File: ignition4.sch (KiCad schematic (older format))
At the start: 9 parts, among them P10 CONN_1, P11 CONN_1, Q3 MOSFET_N, SW3 SWITCH_INV

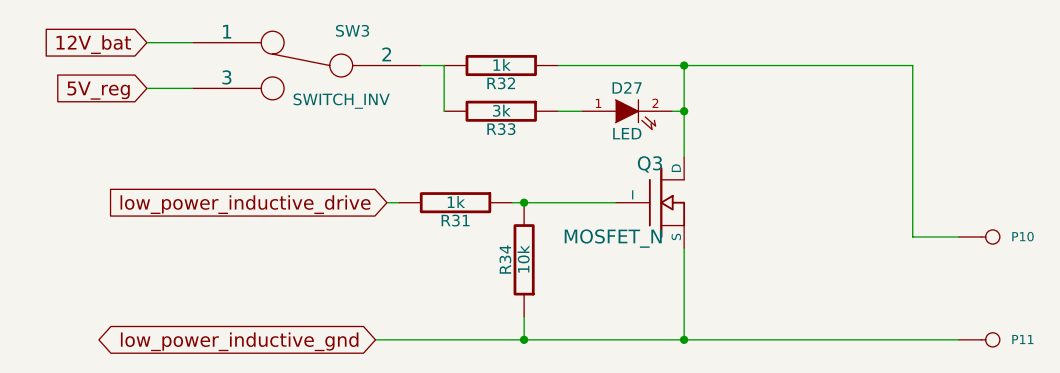
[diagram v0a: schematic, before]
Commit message: DFH mans up a bit. Perhaps usable for something at this point, like making trips to the local store ;)
I connected TA pins to sub circuits, fixed a number if items discussed in the DIYEFI forums. This is it's 21st version, so it was time for it to man up a bit, and become something potentially useful.

Signed-off-by: Jared Harvey <TortiseGIT@jaredharvey.com>
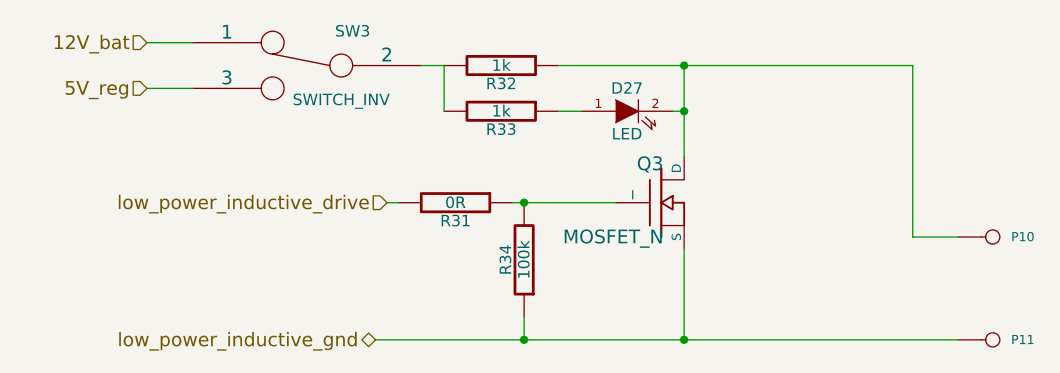
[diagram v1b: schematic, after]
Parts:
- D27: A (none) -> 10mA; V (none) -> 12V; construct (none) -> LED with resistor included; misc (none) -> other,more,stuff; vend1,smd e hem (none) -> newark,; vend2, smd w hem (none) -> digi,; vend2, thru w hem (none) -> digi,; vendor1, thru e hem (none) -> newark,58K2517
- Q3: A (none) -> 28A; V (none) -> 42V; construct (none) -> OVP protected MOSFET; misc (none) -> other,more,stuff; vend1,smd e hem (none) -> newark,; vend2, smd w hem (none) -> digi,; vend2, thru w hem (none) -> digi,VNP28N04-E-ND; vendor1, thru e hem (none) -> element14,1739427
- R31: value 1k -> 0R; TOL (none) -> 5%; W (none) -> 1/4W; construct (none) -> carbon film; misc (none) -> other,more,stuff; vend1,smd e hem (none) -> newark,36C9353; vend2, smd w hem (none) -> digi,CRCW08050000ZSTA-ND; vend2, thru w hem (none) -> digi,604HR025E-ND; vendor1, thru e hem (none) -> newark,64K9335
- R32: W (none) -> 1/4w; construct (none) -> carbon film; misc (none) -> other,more,stuff; tol (none) -> 5%; vend1,smd e hem (none) -> newark,52K9725; vend2, smd w hem (none) -> digi,CRCW08051K00JNEA; vend2, thru w hem (none) -> digi,OD102J-ND; vendor1, thru e hem (none) -> newark,65K2365
- R33: value 3k -> 1k; W (none) -> 1/4w; construct (none) -> carbon film; misc (none) -> other,more,stuff; tol (none) -> 5%; vend1,smd e hem (none) -> newark,52K9725; vend2, smd w hem (none) -> digi,CRCW08051K00JNEA; vend2, thru w hem (none) -> digi,OD102J-ND; vendor1, thru e hem (none) -> newark,65K2365
- R34: value 10k -> 100k; Field10 (none) -> carbon film; Field11 (none) -> other,more,stuff; Field4 (none) -> newark,38k0328; Field5 (none) -> vendor1, smd w hem; Field6 (none) -> vendor2, thru w hem; Field7 (none) -> vendor2, smd w hem; Field8 (none) -> 250,mW; Field9 (none) -> 5,%
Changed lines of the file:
@@
-EESchema Schematic File Version 1
-LIBS:power,./freeEMS_lib,device,conn,linear,regul,74xx,cmos4000,adc-dac,memory,xilinx,special,microcontrollers,dsp,microchip,analog_switches,motorola,texas,intel,audio,interface,digital-audio,philips,display,cypress,siliconi,contrib,valves,./freeEMS_1.cache
-EELAYER 23  0
+EESchema Schematic File Version 2  date 9/10/2011 11:43:50 AM
+LIBS:power
+LIBS:freeEMS_lib
+LIBS:device
+LIBS:conn
+LIBS:linear
+LIBS:regul
+LIBS:74xx
+LIBS:cmos4000
+LIBS:adc-dac
+LIBS:memory
+LIBS:xilinx
+LIBS:special
+LIBS:microcontrollers
+LIBS:dsp
+LIBS:microchip
+LIBS:analog_switches
+LIBS:motorola
+LIBS:texas
+LIBS:intel
+LIBS:audio
+LIBS:interface
+LIBS:digital-audio
+LIBS:philips
+LIBS:display
+LIBS:cypress
+LIBS:siliconi
+LIBS:contrib
+LIBS:valves
+LIBS:freeEMS_1-cache
+EELAYER 25  0
 EELAYER END
 $Descr A4 11700 8267
+encoding utf-8
 Sheet 12 41
-Title "freeEMS 1.0"
-Date "15 nov 2008"
-Rev "A.20"
-Comp "diyefi.org"
+Title "DFH for freeEMS"
+Date "10 sep 2011"
+Rev "A.21"
+Comp "FreeEMS.org"
 Comment1 "ignition.sch"
 Comment2 ""
@@
 $Comp
 L PIP-3104 Q3
-U 1 1 48B16ED5
+U 1 1 4E6B707C
 P 4000 2050
-F 0 "Q3" H 4010 2220 60  0000 R C
-F 1 "MOSFET_N" H 4010 1900 60  0000 R C
-F 2 "TO220_sm" V 3930 2800 60  0001 C C
-F 4 "digi,PIP3104-ND" V 2130 3800 60  0001 C C
-F 5 "vendor1, smd w hem" V 2130 3800 60  0001 C C
-F 6 "vendor2, thru w hem" V 2130 3800 60  0001 C C
-F 7 "vendor2, smd w hem" V 2130 3800 60  0001 C C
-F 8 "8,A" V 2130 3800 60  0001 C C
-F 9 "x,x" V 2130 3800 60  0001 C C
-F 10 "TOPFET" V 2130 3800 60  0001 C C
-F 11 "other,more,stuff" V 2130 3800 60  0001 C C
+F 0 "Q3" H 4010 2220 60  0000 R CNN
+F 1 "MOSFET_N" H 4010 1900 60  0000 R CNN
+F 2 "TO220_sm" V 1130 2600 60  0001 C CNN
+F 4 "element14,1739427" V 1130 2600 60  0001 C CNN "vendor1, thru e hem"
+F 5 "newark," V 1130 2600 60  0001 C CNN "vend1,smd e hem"
+F 6 "digi,VNP28N04-E-ND" V 1130 2600 60  0001 C CNN "vend2, thru w hem"
+F 7 "digi," V 1130 2600 60  0001 C CNN "vend2, smd w hem"
+F 8 "28A" V 1130 2600 60  0001 C CNN "A"
+F 9 "42V" V 1130 2600 60  0001 C CNN "V"
+F 10 "OVP protected MOSFET" V 1130 2600 60  0001 C CNN "construct"
+F 11 "other,more,stuff" V 1130 2600 60  0001 C CNN "misc"
 	1    4000 2050
 	1    0    0    -1
@@
 $Comp
 L R R34
-U 1 1 48AE08BB
+U 1 1 4E6B706E
 P 3400 2300
-F 0 "R34" V 3480 2300 50  0000 C C
-F 1 "10k" V 3400 2300 50  0000 C C
-F 2 "R4-SM0805" V 3580 2400 60  0001 C C
-F 4 "newark,38k0328" V 1230 2850 60  0001 C C
-F 5 "vendor1, smd w hem" V 1230 2850 60  0001 C C
-F 6 "vendor2, thru w hem" V 1230 2850 60  0001 C C
-F 7 "vendor2, smd w hem" V 1230 2850 60  0001 C C
-F 8 "250,mW" V 1230 2850 60  0001 C C
-F 9 "5,%" V 1230 2850 60  0001 C C
-F 10 "carbon film" V 1230 2850 60  0001 C C
-F 11 "other,more,stuff" V 1230 2850 60  0001 C C
+F 0 "R34" V 3480 2300 50  0000 C CNN
+F 1 "100k" V 3400 2300 50  0000 C CNN
+F 2 "R4-SM0805" V 3580 2400 60  0001 C CNN
+F 4 "newark,38k0328" V 1230 2850 60  0001 C CNN "Field4"
+F 5 "vendor1, smd w hem" V 1230 2850 60  0001 C CNN "Field5"
+F 6 "vendor2, thru w hem" V 1230 2850 60  0001 C CNN "Field6"
+F 7 "vendor2, smd w hem" V 1230 2850 60  0001 C CNN "Field7"
+F 8 "250,mW" V 1230 2850 60  0001 C CNN "Field8"
+F 9 "5,%" V 1230 2850 60  0001 C CNN "Field9"
+F 10 "carbon film" V 1230 2850 60  0001 C CNN "Field10"
+F 11 "other,more,stuff" V 1230 2850 60  0001 C CNN "Field11"
 	1    3400 2300
 	-1   0    0    1
@@
 $Comp
 L SWITCH_INV SW3
-U 1 1 48AE0832
+U 1 1 4E6B7068
 P 2450 1450
-F 0 "SW3" H 2250 1600 50  0000 C C
-F 1 "SWITCH_INV" H 2300 1300 50  0000 C C
-F 2 "SIL-3" H 2350 1700 60  0001 C C
+F 0 "SW3" H 2250 1600 50  0000 C CNN
+F 1 "SWITCH_INV" H 2300 1300 50  0000 C CNN
+F 2 "SIL-3" H 2350 1700 60  0001 C CNN
 	1    2450 1450
 	-1   0    0    -1
@@
 $Comp
 L LED D27
-U 1 1 48AA2529
+U 1 1 4E6B7054
 P 3850 1650
-F 0 "D27" H 3850 1750 50  0000 C C
-F 1 "LED" H 3850 1550 50  0000 C C
-F 2 "LEDV" V 1680 5050 60  0001 C C
-F 4 "newark,58k2469" V 430 2100 60  0001 C C
-F 5 "vendor1, smd w hem" V 430 2100 60  0001 C C
-F 6 "vendor2, thru w hem" V 430 2100 60  0001 C C
-F 7 "vendor2, smd w hem" V 430 2100 60  0001 C C
-F 8 "x,x" V 430 2100 60  0001 C C
-F 9 "x,x" V 430 2100 60  0001 C C
-F 10 "green" V 430 2100 60  0001 C C
-F 11 "other,more,stuff" V 430 2100 60  0001 C C
+F 0 "D27" H 3850 1750 50  0000 C CNN
+F 1 "LED" H 3850 1550 50  0000 C CNN
+F 2 "LEDV" V 1130 2600 60  0001 C CNN
+F 4 "newark,58K2517" V 1130 2600 60  0001 C CNN "vendor1, thru e hem"
+F 5 "newark," V 1130 2600 60  0001 C CNN "vend1,smd e hem"
+F 6 "digi," V 1130 2600 60  0001 C CNN "vend2, thru w hem"
+F 7 "digi," V 1130 2600 60  0001 C CNN "vend2, smd w hem"
+F 8 "10mA" V 1130 2600 60  0001 C CNN "A"
+F 9 "12V" V 1130 2600 60  0001 C CNN "V"
+F 10 "LED with resistor included" V 1130 2600 60  0001 C CNN "construct"
+F 11 "other,more,stuff" V 1130 2600 60  0001 C CNN "misc"
 	1    3850 1650
 	1    0    0    -1
@@
 $Comp
 L R R33
-U 1 1 48AA2523
+U 1 1 4E6B704F
 P 3300 1650
-F 0 "R33" V 3380 1650 50  0000 C C
-F 1 "3k" V 3300 1650 50  0000 C C
-F 2 "R4-SM0805" V 1980 1650 60  0001 C C
-F 4 "newark,38k0340" V -120 2400 60  0001 C C
-F 5 "vendor1, smd w hem" V -120 2400 60  0001 C C
-F 6 "vendor2, thru w hem" V -120 2400 60  0001 C C
-F 7 "vendor2, smd w hem" V -120 2400 60  0001 C C
-F 8 "1/4,W" V -120 2400 60  0001 C C
-F 9 "5,%" V -120 2400 60  0001 C C
-F 10 "carbon film" V -120 2400 60  0001 C C
-F 11 "other,more,stuff" V -120 2400 60  0001 C C
+F 0 "R33" V 3380 1650 50  0000 C CNN
+F 1 "1k" V 3300 1650 50  0000 C CNN
+F 2 "R4-SM0805" V 1130 2600 60  0001 C CNN
+F 4 "newark,65K2365" V 1130 2600 60  0001 C CNN "vendor1, thru e hem"
+F 5 "newark,52K9725" V 1130 2600 60  0001 C CNN "vend1,smd e hem"
+F 6 "digi,OD102J-ND" V 1130 2600 60  0001 C CNN "vend2, thru w hem"
+F 7 "digi,CRCW08051K00JNEA" V 1130 2600 60  0001 C CNN "vend2, smd w hem"
+F 8 "1/4w" V 1130 2600 60  0001 C CNN "W"
+F 9 "5%" V 1130 2600 60  0001 C CNN "tol"
+F 10 "carbon film" V 1130 2600 60  0001 C CNN "construct"
+F 11 "other,more,stuff" V 1130 2600 60  0001 C CNN "misc"
 	1    3300 1650
 	0    1    1    0
@@
 $Comp
 L CONN_1 P11
-U 1 1 48AA1A4E
+U 1 1 4E6B7039
 P 5450 2650
-F 0 "P11" H 5530 2650 40  0000 L C
-F 1 "CONN_1" H 5450 2705 30  0001 C C
-F 2 "1PIN" V 1880 2850 60  0001 C C
+F 0 "P11" H 5530 2650 40  0000 L CNN
+F 1 "CONN_1" H 5450 2705 30  0001 C CNN
+F 2 "1PIN" V 1880 2850 60  0001 C CNN
 	1    5450 2650
 	1    0    0    -1
@@
 $Comp
 L CONN_1 P10
-U 1 1 48AA1A4A
+U 1 1 4E6B7035
 P 5450 2200
-F 0 "P10" H 5530 2200 40  0000 L C
-F 1 "CONN_1" H 5450 2255 30  0001 C C
-F 2 "1PIN" V 1880 2600 60  0001 C C
+F 0 "P10" H 5530 2200 40  0000 L CNN
+F 1 "CONN_1" H 5450 2255 30  0001 C CNN
+F 2 "1PIN" V 1880 2600 60  0001 C CNN
 	1    5450 2200
 	1    0    0    -1
 $EndComp
-Text GLabel 1750 1550 0    60   Input
+Text HLabel 1750 1550 0    60   Input ~ 0
 5V_reg
 $Comp
 L R R31
-U 1 1 489395E6
+U 1 1 4E6B7004
 P 3100 2050
-F 0 "R31" V 3180 2050 50  0000 C C
-F 1 "1k" V 3100 2050 50  0000 C C
-F 2 "R4-SM0805" V 3280 2150 60  0001 C C
-F 4 "newark,38k0327" V 930 2600 60  0001 C C
-F 5 "vendor1, smd w hem" V 930 2600 60  0001 C C
-F 6 "vendor2, thru w hem" V 930 2600 60  0001 C C
-F 7 "vendor2, smd w hem" V 930 2600 60  0001 C C
-F 8 "250,mW" V 930 2600 60  0001 C C
-F 9 "5,%" V 930 2600 60  0001 C C
-F 10 "carbon film" V 930 2600 60  0001 C C
-F 11 "other,more,stuff" V 930 2600 60  0001 C C
+F 0 "R31" V 3180 2050 50  0000 C CNN
+F 1 "0R" V 3100 2050 50  0000 C CNN
+F 2 "R4-SM0805" V 1130 2600 60  0001 C CNN
+F 4 "newark,64K9335" V 1130 2600 60  0001 C CNN "vendor1, thru e hem"
+F 5 "newark,36C9353" V 1130 2600 60  0001 C CNN "vend1,smd e hem"
+F 6 "digi,604HR025E-ND" V 1130 2600 60  0001 C CNN "vend2, thru w hem"
+F 7 "digi,CRCW08050000ZSTA-ND" V 1130 2600 60  0001 C CNN "vend2, smd w hem"
+F 8 "1/4W" V 1130 2600 60  0001 C CNN "W"
+F 9 "5%" V 1130 2600 60  0001 C CNN "TOL"
+F 10 "carbon film" V 1130 2600 60  0001 C CNN "construct"
+F 11 "other,more,stuff" V 1130 2600 60  0001 C CNN "misc"
 	1    3100 2050
 	0    1    1    0
@@
 $Comp
 L R R32
-U 1 1 489395D4
+U 1 1 4E6B6FFC
 P 3300 1450
-F 0 "R32" V 3380 1450 50  0000 C C
-F 1 "1k" V 3300 1450 50  0000 C C
-F 2 "R4-SM0805" V 3480 1550 60  0001 C C
-F 4 "newark,38k0327" V 1130 2350 60  0001 C C
-F 5 "vendor1, smd w hem" V 1130 2350 60  0001 C C
-F 6 "vendor2, thru w hem" V 1130 2350 60  0001 C C
-F 7 "vendor2, smd w hem" V 1130 2350 60  0001 C C
-F 8 "250,mW" V 1130 2350 60  0001 C C
-F 9 "5,%" V 1130 2350 60  0001 C C
-F 10 "carbon film" V 1130 2350 60  0001 C C
-F 11 "other,more,stuff" V 1130 2350 60  0001 C C
+F 0 "R32" V 3380 1450 50  0000 C CNN
+F 1 "1k" V 3300 1450 50  0000 C CNN
+F 2 "R4-SM0805" V 1130 2600 60  0001 C CNN
+F 4 "newark,65K2365" V 1130 2600 60  0001 C CNN "vendor1, thru e hem"
+F 5 "newark,52K9725" V 1130 2600 60  0001 C CNN "vend1,smd e hem"
+F 6 "digi,OD102J-ND" V 1130 2600 60  0001 C CNN "vend2, thru w hem"
+F 7 "digi,CRCW08051K00JNEA" V 1130 2600 60  0001 C CNN "vend2, smd w hem"
+F 8 "1/4w" V 1130 2600 60  0001 C CNN "W"
+F 9 "5%" V 1130 2600 60  0001 C CNN "tol"
+F 10 "carbon film" V 1130 2600 60  0001 C CNN "construct"
+F 11 "other,more,stuff" V 1130 2600 60  0001 C CNN "misc"
 	1    3300 1450
 	0    1    1    0
 $EndComp
-Text GLabel 1750 1350 0    60   Input
+Text HLabel 1750 1350 0    60   Input ~ 0
 12V_bat
-Text GLabel 2750 2650 0    60   BiDi
+Text HLabel 2750 2650 0    60   BiDi ~ 0
 low_power_inductive_gnd
-Text GLabel 2800 2050 0    60   Input
+Text HLabel 2800 2050 0    60   Input ~ 0
 low_power_inductive_drive
 $EndSCHEMATC
